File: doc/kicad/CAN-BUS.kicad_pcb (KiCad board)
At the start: 2 copper layers, 18 parts, among them K1 HFD2_005-S-L2-D, U1 PCF8574, U10 MCP2551-I-SN, U11 MCP2515-xSO, U2 PCF8574, U3 PCF8574, U4 ULN2803A, U5 ULN2803A, U6 ULN2803A, U7 ULN2803A, U8 ULN2803A

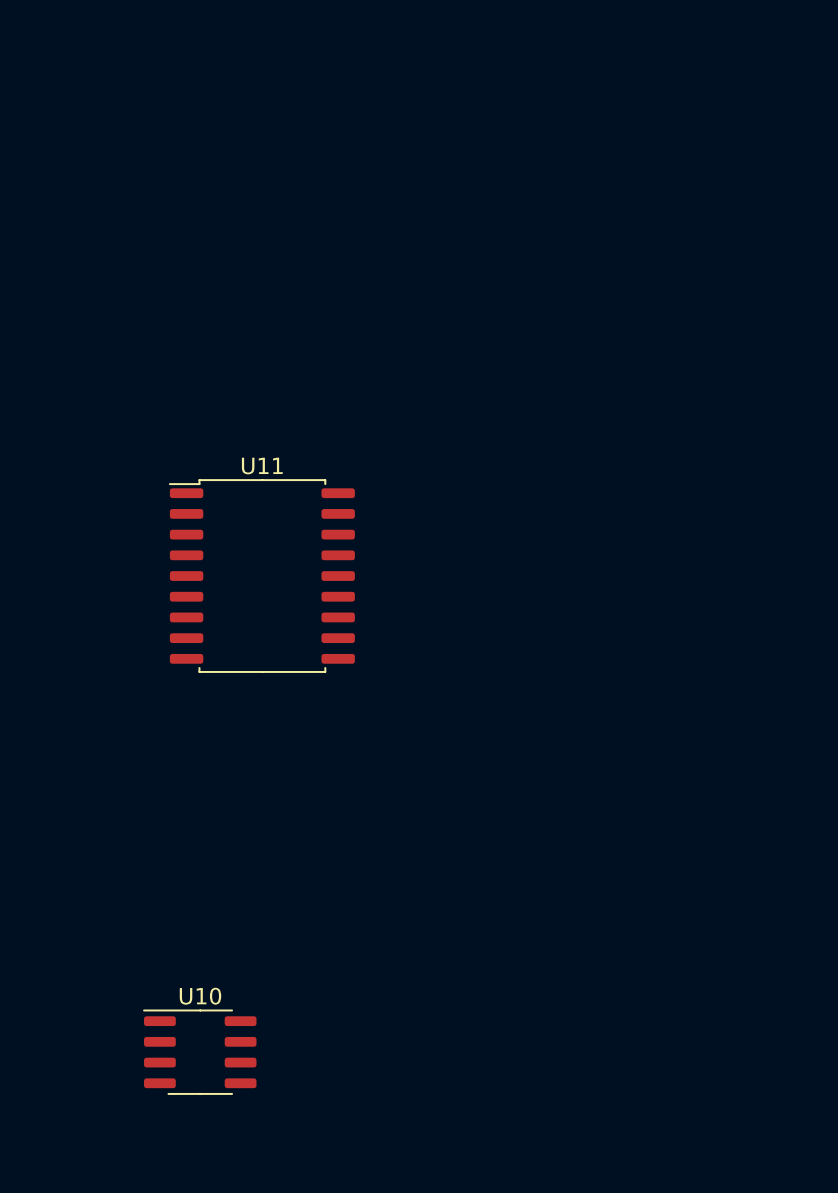
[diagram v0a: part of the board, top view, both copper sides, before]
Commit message: Schaltplan angepasst
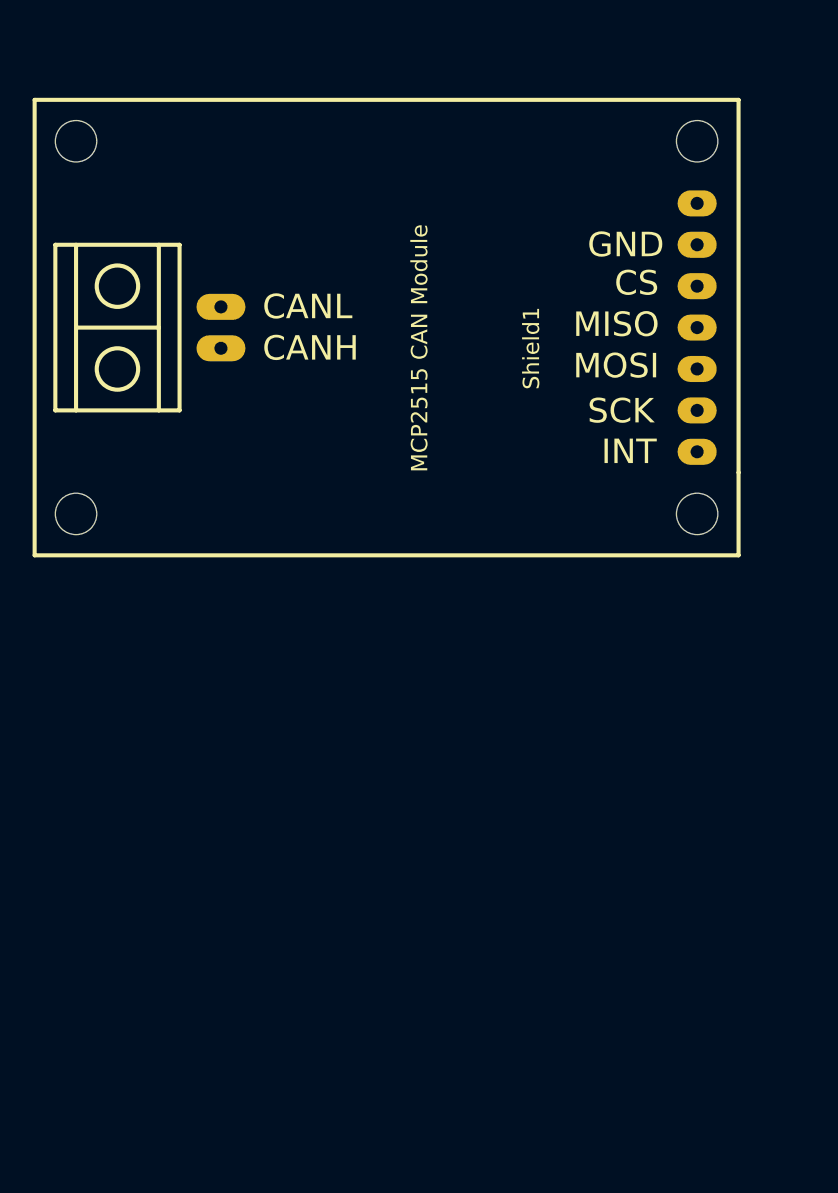
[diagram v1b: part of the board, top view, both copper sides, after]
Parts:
- removed U10: MCP2551-I-SN, Package_SO:SOIC-8_3.9x4.9mm_P1.27mm
- removed U11: MCP2515-xSO, Package_SO:SOIC-18W_7.5x11.6mm_P1.27mm
- added Shield1: CAN-BUS_MODULE_TJA1050, kicad-lib:MCP2515_CAN_MODULE_BY0-10, F.Cu at (55.9, 53.3)
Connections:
- A1 pad 1: Net-(A1-Pad1) -> (no net)
- A1 pad 17: Net-(A1-Pad17) -> (no net)
- A1 pad 18: Net-(A1-Pad18) -> (no net)
- A1 pad 2: Net-(A1-Pad2) -> (no net)
- A1 pad 26: Net-(A1-Pad26) -> (no net)
- A1 pad 28: Net-(A1-Pad28) -> (no net)
- A1 pad 3: Net-(A1-Pad3) -> (no net)
- A1 pad 30: Net-(A1-Pad30) -> (no net)
- A1 pad 6: Net-(A1-Pad6) -> (no net)
- K1 pad 1: Net-(K1-Pad1) -> (no net)
- K1 pad 11: Net-(K1-Pad11) -> (no net)
- K1 pad 13: Net-(K1-Pad13) -> (no net)
- K1 pad 15: Net-(K1-Pad15) -> (no net)
- K1 pad 16: Net-(K1-Pad16) -> (no net)
- K1 pad 2: Net-(K1-Pad2) -> (no net)
- K1 pad 4: Net-(K1-Pad4) -> (no net)
- K1 pad 6: Net-(K1-Pad6) -> (no net)
- K1 pad 8: Net-(K1-Pad8) -> (no net)
- K1 pad 9: Net-(K1-Pad9) -> (no net)
- U1 pad 13: Net-(U1-Pad13) -> (no net)
- U2 pad 13: Net-(U2-Pad13) -> (no net)
- U3 pad 13: Net-(U3-Pad13) -> (no net)
- U4 pad 10: Net-(U4-Pad10) -> (no net)
- U4 pad 11: Net-(U4-Pad11) -> (no net)
- U4 pad 12: Net-(U4-Pad12) -> (no net)
- U4 pad 13: Net-(U4-Pad13) -> (no net)
- U4 pad 14: Net-(U4-Pad14) -> (no net)
- U4 pad 15: Net-(U4-Pad15) -> (no net)
- U4 pad 16: Net-(U4-Pad16) -> (no net)
- U4 pad 17: Net-(U4-Pad17) -> (no net)
- U4 pad 18: Net-(U4-Pad18) -> (no net)
- U5 pad 10: Net-(U5-Pad10) -> (no net)
- U5 pad 11: Net-(U5-Pad11) -> (no net)
- U5 pad 12: Net-(U5-Pad12) -> (no net)
- U5 pad 13: Net-(U5-Pad13) -> (no net)
- U5 pad 14: Net-(U5-Pad14) -> (no net)
- U5 pad 15: Net-(U5-Pad15) -> (no net)
- U5 pad 16: Net-(U5-Pad16) -> (no net)
- U5 pad 17: Net-(U5-Pad17) -> (no net)
- U5 pad 18: Net-(U5-Pad18) -> (no net)
- U6 pad 10: Net-(U6-Pad10) -> (no net)
- U6 pad 11: Net-(U6-Pad11) -> (no net)
- U6 pad 12: Net-(U6-Pad12) -> (no net)
- U6 pad 13: Net-(U6-Pad13) -> (no net)
- U6 pad 14: Net-(U6-Pad14) -> (no net)
- U6 pad 15: Net-(U6-Pad15) -> (no net)
- U6 pad 16: Net-(U6-Pad16) -> (no net)
- U6 pad 17: Net-(U6-Pad17) -> (no net)
- U6 pad 18: Net-(U6-Pad18) -> (no net)
- U7 pad 10: Net-(U7-Pad10) -> (no net)
- U7 pad 11: Net-(U7-Pad11) -> (no net)
- U7 pad 12: Net-(U7-Pad12) -> (no net)
- U7 pad 13: Net-(U7-Pad13) -> (no net)
- U7 pad 14: Net-(U7-Pad14) -> (no net)
- U7 pad 15: Net-(U7-Pad15) -> (no net)
- U7 pad 16: Net-(U7-Pad16) -> (no net)
- U7 pad 17: Net-(U7-Pad17) -> (no net)
- U7 pad 18: Net-(U7-Pad18) -> (no net)
- U8 pad 10: Net-(U8-Pad10) -> (no net)
- U8 pad 11: Net-(U8-Pad11) -> (no net)
- U8 pad 12: Net-(U8-Pad12) -> (no net)
- U8 pad 13: Net-(U8-Pad13) -> (no net)
- U8 pad 14: Net-(U8-Pad14) -> (no net)
- U8 pad 15: Net-(U8-Pad15) -> (no net)
- U8 pad 16: Net-(U8-Pad16) -> (no net)
- U8 pad 17: Net-(U8-Pad17) -> (no net)
- U8 pad 18: Net-(U8-Pad18) -> (no net)
- U8 pad 3: Net-(U8-Pad3) -> (no net)
- U8 pad 4: Net-(U8-Pad4) -> (no net)
- U8 pad 5: Net-(U8-Pad5) -> (no net)
- U8 pad 6: Net-(U8-Pad6) -> (no net)
- U8 pad 7: Net-(U8-Pad7) -> (no net)
- U8 pad 8: Net-(U8-Pad8) -> (no net)
- U8 pad 9: Net-(U8-Pad9) -> (no net)

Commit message: initial
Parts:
- added C1: 100n, Capacitors_THT:C_Disc_D7.0mm_W2.5mm_P5.00mm, F.Cu at (124.6, 125.3)
- added C2: 100n, Capacitors_THT:C_Disc_D7.0mm_W2.5mm_P5.00mm, F.Cu at (90.3, 10.5)
- added C3: 100n, Capacitors_THT:C_Disc_D7.0mm_W2.5mm_P5.00mm, F.Cu at (124.6, 121.0)
- added J1: RJ45_LED_Shielded, Connectors:RJ45_TRANSFO, F.Cu at (-59.7, 54.6)
- added J2: RJ45_Shielded, Connectors:RJ45_8, F.Cu at (-50.8, 74.9)
- added R4: 4k7, Resistors_SMD:R_0603, F.Cu at (147.3, 109.2)
- added R5: 4k7, Resistors_SMD:R_0603, F.Cu at (115.6, 100.3)
- added R6: 1K, Resistors_SMD:R_0603, F.Cu at (-27.9, 66.0)
- moved K1 160.2 mm to (25.4, 115.6)
- moved U3 94.2 mm to (190.5, 101.6), turned to 180 degrees
- moved U6 92.0 mm to (199.4, 83.8), turned to 0 degrees
- moved U4 78.8 mm to (190.5, 162.6), turned to 180 degrees
- moved U2 73.8 mm to (148.6, 27.9)
- moved U1 60.4 mm to (99.1, 47.0)
- moved U7 55.9 mm to (199.4, 144.8), turned to 0 degrees
- moved U5 34.7 mm to (190.5, 132.1), turned to 180 degrees
- moved U8 18.9 mm to (199.4, 114.3), turned to 0 degrees
- moved Shield1 16.6 mm to (72.4, 52.1)
- moved A1 4.02 mm to (132.1, 55.9)
- renumbered JP3 to JP2, JP1 to JP3, JP2 to JP4, R3 to R1, R1 to R3, U7 to U1, U8 to U2, U1 to U3, U2 to U4, U3 to U5, U4 to U6, U5 to U7, U6 to U8
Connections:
- Shield1 pad H: (no net) -> Net-(J1-Pad1)
- Shield1 pad L: (no net) -> Net-(J1-Pad2)
- U1 pad 1: Net-(A1-Pad7) -> Net-(A1-Pad19)
- U1 pad 2: Net-(A1-Pad8) -> Net-(A1-Pad20)
- U1 pad 3: Net-(A1-Pad9) -> Net-(A1-Pad12)
- U1 pad 4: Net-(A1-Pad10) -> Net-(A1-Pad11)
- U1 pad 5: Net-(A1-Pad11) -> Net-(A1-Pad10)
- U1 pad 6: Net-(A1-Pad12) -> Net-(A1-Pad9)
- U1 pad 7: Net-(A1-Pad19) -> Net-(A1-Pad8)
- U1 pad 8: Net-(A1-Pad20) -> Net-(A1-Pad7)
- U2 pad 9: (no net) -> GND
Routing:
- net GND: track 0.00 -> 212.0 mm
- net +5V: track 0.00 -> 94.6 mm
- net Net-(A1-Pad23): track 0.00 -> 83.1 mm
- net Net-(A1-Pad24): track 0.00 -> 83.1 mm
- net Net-(A1-Pad5): track 0.00 -> 63.9 mm
- net Net-(A1-Pad13): track 0.00 -> 37.1 mm
- net Net-(J1-Pad2): track 0.00 -> 36.7 mm
- net Net-(A1-Pad14): track 0.00 -> 35.2 mm
- net Net-(J1-Pad1): track 0.00 -> 34.9 mm
- net Net-(J1-Pad5): track 0.00 -> 34.3 mm
- net Net-(U5-Pad9): track 0.00 -> 31.3 mm
- net Net-(A1-Pad15): track 0.00 -> 30.9 mm
- net Net-(U4-Pad9): track 0.00 -> 30.6 mm
- net Net-(J1-Pad4): track 0.00 -> 29.8 mm
- net Net-(A1-Pad16): track 0.00 -> 26.7 mm
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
